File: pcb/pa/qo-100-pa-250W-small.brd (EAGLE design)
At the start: 150 x 100 mm, 2 parts

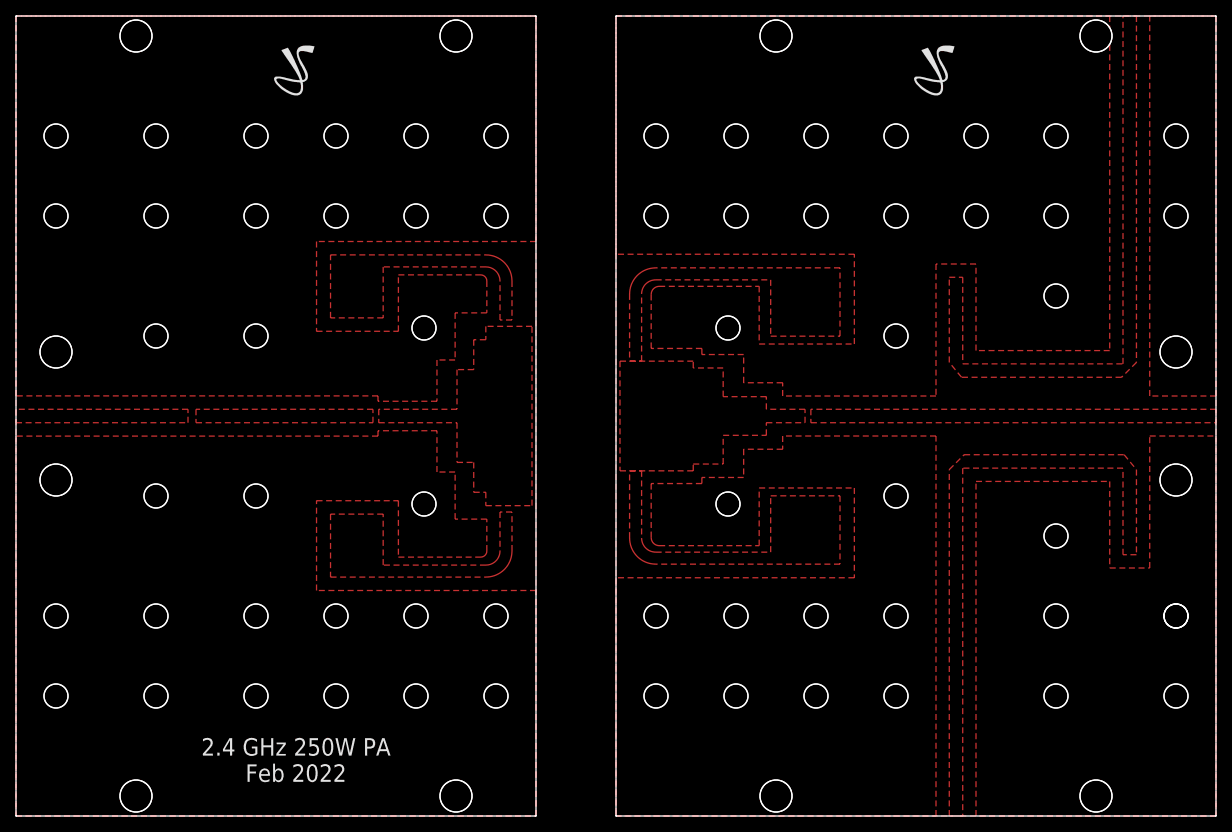
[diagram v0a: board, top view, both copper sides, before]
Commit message: Changes to 250W PA Added smaller version of 250W PA
Signed-off-by: João Silva <jgc3silva@gmail.com>
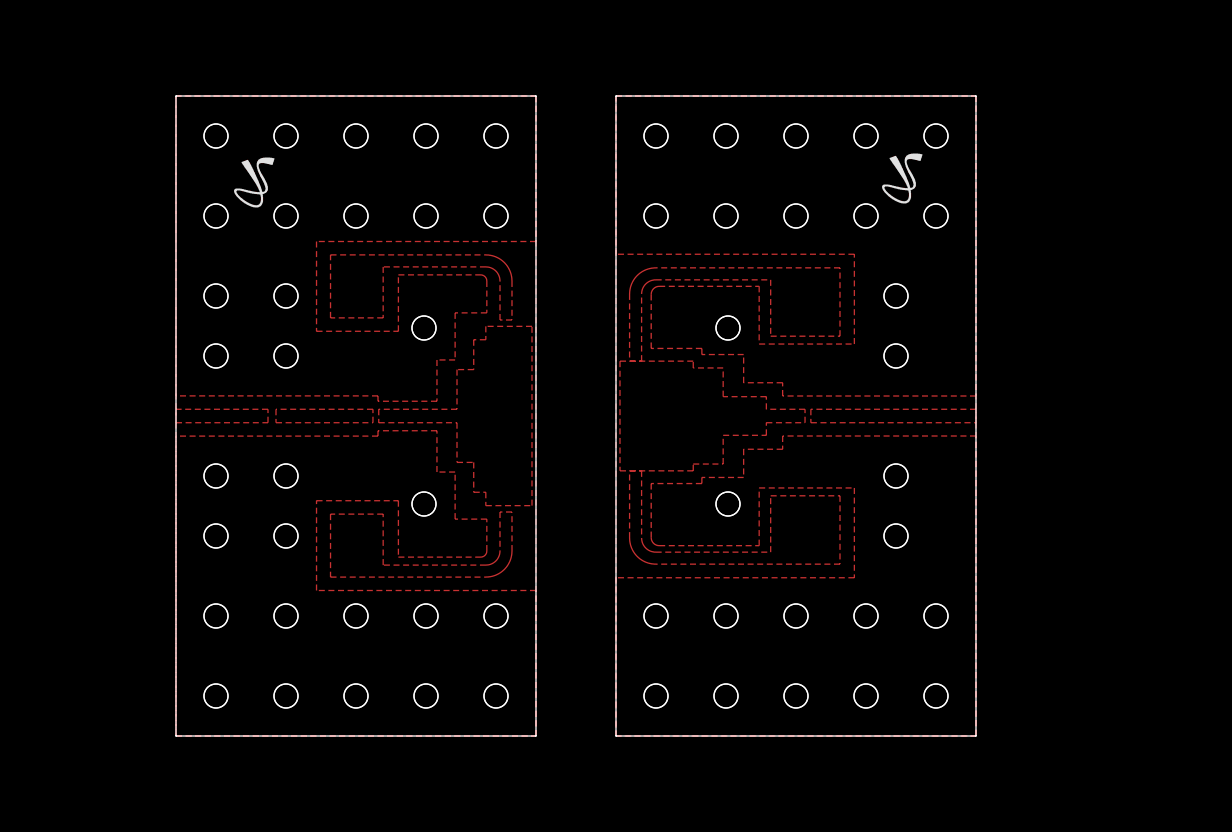
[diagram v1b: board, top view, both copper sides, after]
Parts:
- moved E$2 14.9 mm to (-37.5, 32.5)
- moved E$1 14.1 mm to (43.5, 33.0)
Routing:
- removed copper zone on layer 1, net FWD
- removed copper zone on layer 1, net FWD1
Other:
- board size 150 x 100 mm -> 100 x 80 mm
- board text removed: "2.4 GHz 250W PA Feb 2022"
